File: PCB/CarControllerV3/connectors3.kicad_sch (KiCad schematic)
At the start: 41 parts, among them J5 649012227222, J6 61201621621, K2 RT424005, K5 RT424005

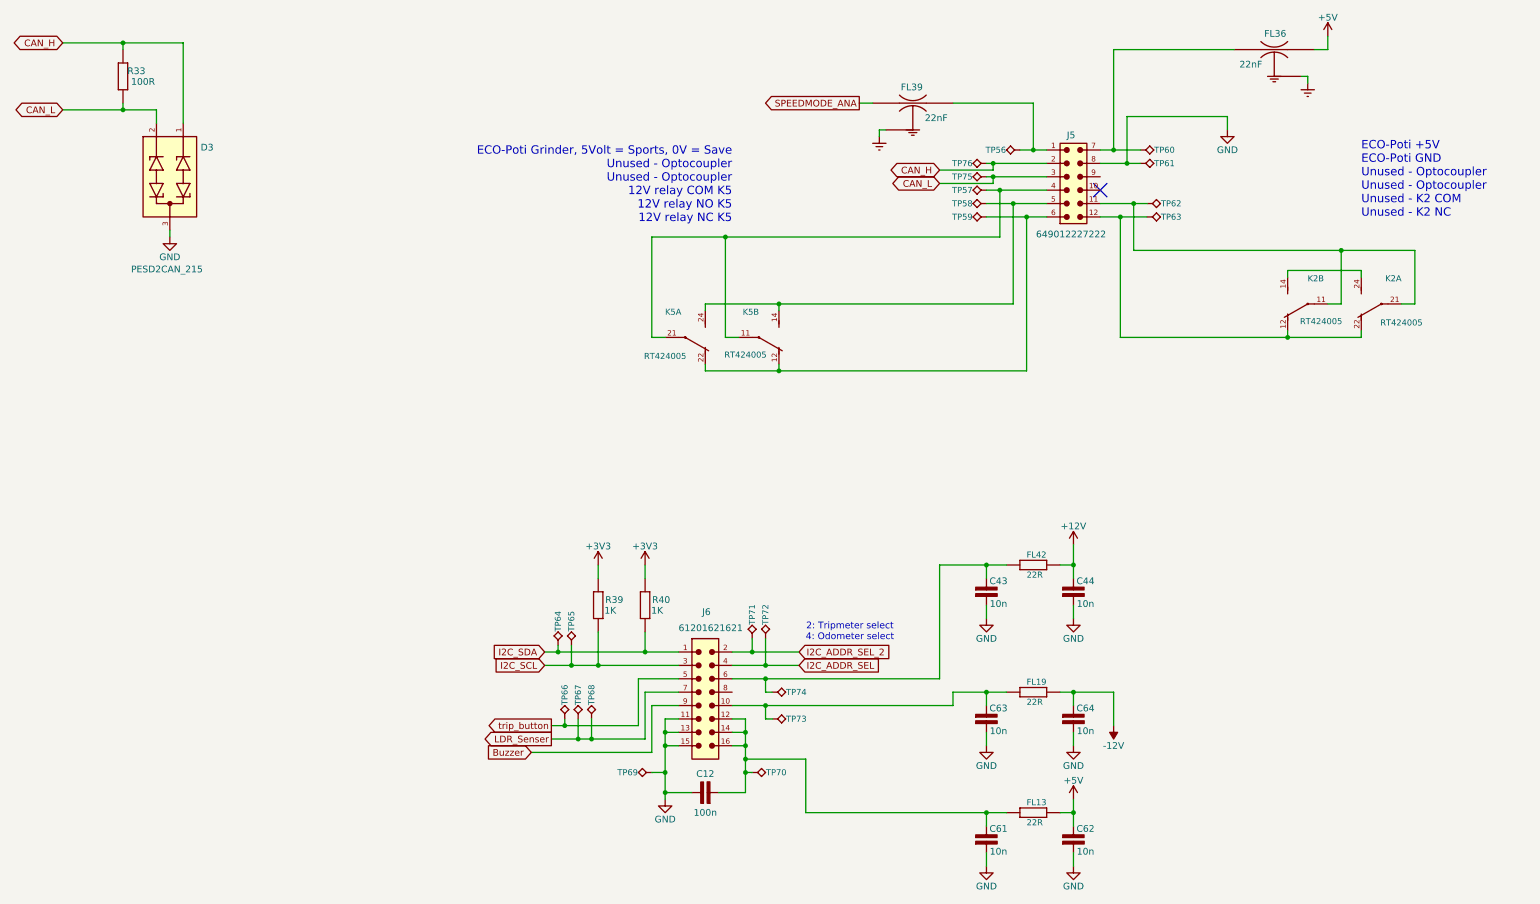
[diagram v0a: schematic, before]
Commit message: More work to PCB
- Rerouted bunch of connections
- Added alternative charge pump circuit
- Bunch of work on analog circuit
- Removed all the capacitor filter on the connectors in favor of filtering when nessesary.
- Placed canbus on JP5.2, JP5.3
- Disconnected various connections that needs to be decided if we should use.
- Added protection to various areas
- Added various todo notes everywhere..
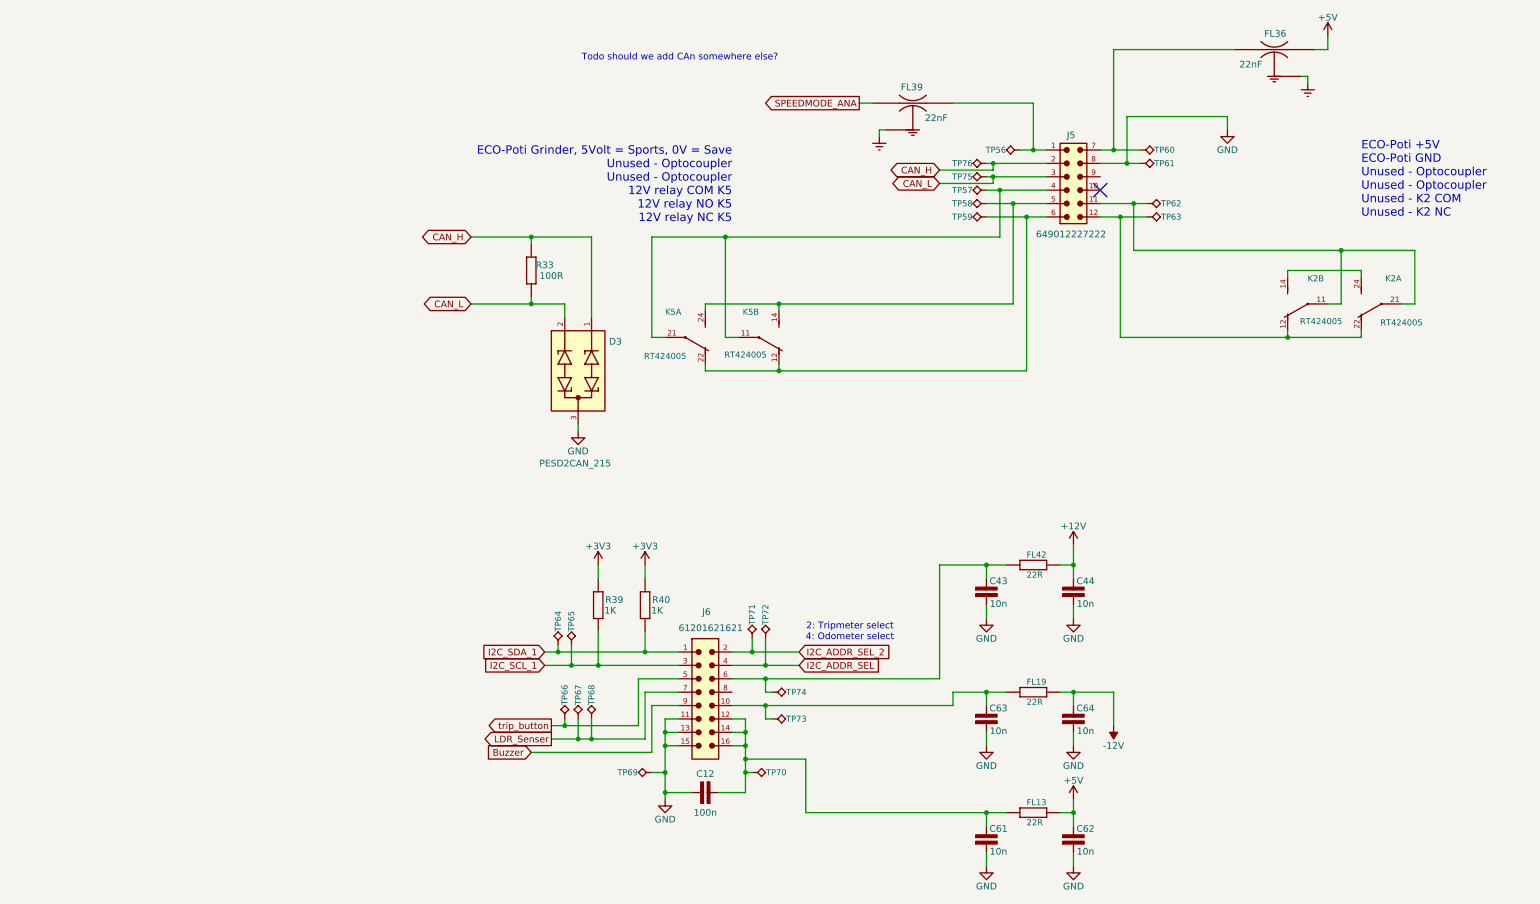
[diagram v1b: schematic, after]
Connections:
- net I2C_SCL renamed I2C_SCL_1
- net I2C_SDA renamed I2C_SDA_1
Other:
- note added: "Todo should we add CAn somewhere else?"
- moved on the sheet: D3, R33
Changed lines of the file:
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@@
 	(generator_version "10.0")
 	(paper "A4")
+	(text "Todo should we add CAn somewhere else?"
+		(exclude_from_sim no)
+		(at 70.104 24.384 0)
+		(effects
+			(font
+				(size 1.27 1.27)
+			)
+		)
+	)
 	(text "ECO-Poti Grinder, 5Volt = Sports, 0V = Save\nUnused - Optocoupler\nUnused - Optocoupler\n12V relay COM K5\n12V relay NO K5\n12V relay NC K5"
 		(exclude_from_sim no)
@@
 	)
 	(junction
-		(at -35.56 21.59)
+		(at 41.91 58.42)
 		(diameter 0)
 		(color 0 0 0 0)
@@
 	)
 	(junction
-		(at -35.56 34.29)
+		(at 41.91 71.12)
 		(diameter 0)
 		(color 0 0 0 0)
@@
 	(wire
 		(pts
-			(xy -29.21 36.83) (xy -29.21 34.29)
+			(xy 48.26 73.66) (xy 48.26 71.12)
 		)
 		(stroke
@@
 	(wire
 		(pts
-			(xy -29.21 34.29) (xy -35.56 34.29)
+			(xy 48.26 71.12) (xy 41.91 71.12)
 		)
 		(stroke
@@
 	(wire
 		(pts
-			(xy -24.13 21.59) (xy -24.13 36.83)
+			(xy 53.34 58.42) (xy 53.34 73.66)
 		)
 		(stroke
@@
 	(wire
 		(pts
-			(xy -35.56 21.59) (xy -24.13 21.59)
+			(xy 41.91 58.42) (xy 53.34 58.42)
 		)
 		(stroke
@@
 	(wire
 		(pts
-			(xy -35.56 34.29) (xy -46.99 34.29)
+			(xy 41.91 71.12) (xy 30.48 71.12)
 		)
 		(stroke
@@
 	(wire
 		(pts
-			(xy -46.99 21.59) (xy -35.56 21.59)
+			(xy 30.48 58.42) (xy 41.91 58.42)
 		)
 		(stroke
@@
 	(wire
 		(pts
-			(xy -35.56 21.59) (xy -35.56 22.86)
+			(xy 41.91 58.42) (xy 41.91 59.69)
 		)
 		(stroke
@@
 	(wire
 		(pts
-			(xy -35.56 33.02) (xy -35.56 34.29)
+			(xy 41.91 69.85) (xy 41.91 71.12)
 		)
 		(stroke
@@
 	(wire
 		(pts
-			(xy -26.67 58.42) (xy -26.67 57.15)
+			(xy 50.8 95.25) (xy 50.8 93.98)
 		)
 		(stroke
@@
 		)
 	)
-	(global_label "I2C_SDA"
+	(global_label "I2C_SDA_1"
 		(shape input)
 		(at 44.45 137.16 180)
@@
 		)
 		(property "Intersheetrefs" "${INTERSHEET_REFS}"
-			(at 33.8448 137.16 0)
+			(at 31.6677 137.16 0)
 			(hide yes)
 			(show_name no)
@@
 	(global_label "CAN_L"
 		(shape bidirectional)
-		(at -46.99 34.29 180)
+		(at 30.48 71.12 180)
 		(fields_autoplaced yes)
 		(effects
@@
 		)
 		(property "Intersheetrefs" "${INTERSHEET_REFS}"
-			(at -56.7713 34.29 0)
+			(at 20.6987 71.12 0)
 			(hide yes)
 			(show_name no)
@@
 		)
 	)
-	(global_label "I2C_SCL"
+	(global_label "I2C_SCL_1"
 		(shape input)
 		(at 44.45 139.7 180)
@@
 		)
 		(property "Intersheetrefs" "${INTERSHEET_REFS}"
-			(at 33.9053 139.7 0)
+			(at 31.7282 139.7 0)
 			(hide yes)
 			(show_name no)
@@
 	(global_label "CAN_H"
 		(shape bidirectional)
-		(at -46.99 21.59 180)
+		(at 30.48 58.42 180)
 		(fields_autoplaced yes)
 		(effects
@@
 		)
 		(property "Intersheetrefs" "${INTERSHEET_REFS}"
-			(at -57.0737 21.59 0)
+			(at 20.3963 58.42 0)
 			(hide yes)
 			(show_name no)
@@
 	(symbol
 		(lib_id "RC0603FR:RC0603FR-07100R")
-		(at -35.56 27.94 90)
+		(at 41.91 64.77 90)
 		(unit 1)
 		(body_style 1)
@@
 		(dnp no)
 		(property "Reference" "R33"
-			(at -33.02 26.924 90)
+			(at 44.45 63.754 90)
 			(show_name no)
 			(do_not_autoplace no)
@@
 		)
 		(property "Value" "100R"
-			(at -31.75 28.956 90)
+			(at 45.72 65.786 90)
 			(show_name no)
 			(do_not_autoplace no)
@@
 		)
 		(property "Footprint" "footprints:RC0603FR-RESC1608X60N"
-			(at -28.575 27.94 0)
+			(at 48.895 64.77 0)
 			(hide yes)
 			(show_name no)
@@
 		)
 		(property "Datasheet" "https://www.farnell.com/datasheets/443971.pdf"
-			(at -26.035 27.94 0)
+			(at 51.435 64.77 0)
 			(hide yes)
 			(show_name no)
@@
 		)
 		(property "Description" "Resistor XXXX 0603 1%"
-			(at -35.56 27.94 0)
+			(at 41.91 64.77 0)
 			(hide yes)
 			(show_name no)
@@
 		)
 		(property "Voltage" "75V"
-			(at -22.225 27.94 0)
+			(at 55.245 64.77 0)
 			(hide yes)
 			(show_name yes)
@@
 		)
 		(property "Tolerance" "1%"
-			(at -20.32 27.94 0)
+			(at 57.15 64.77 0)
 			(hide yes)
 			(show_name yes)
@@
 		)
 		(property "Power" "100mW"
-			(at -18.415 27.94 0)
+			(at 59.055 64.77 0)
 			(hide yes)
 			(show_name yes)
@@
 	(symbol
 		(lib_id "PESD2CAN_215:PESD2CAN_215")
-		(at -26.67 46.99 270)
+		(at 50.8 83.82 270)
 		(unit 1)
 		(body_style 1)
@@
 		(dnp no)
 		(property "Reference" "D3"
-			(at -20.828 42.164 90)
+			(at 56.642 78.994 90)
 			(show_name no)
 			(do_not_autoplace no)
@@
 		)
 		(property "Value" "PESD2CAN_215"
-			(at -34.036 65.278 90)
+			(at 43.434 102.108 90)
 			(show_name no)
 			(do_not_autoplace no)
@@
 		)
 		(property "Footprint" "footprints:IC_PESD2CAN_215"
-			(at -26.67 46.99 0)
+			(at 50.8 83.82 0)
 			(hide yes)
 			(show_name no)
@@
 		)
 		(property "Datasheet" ""
-			(at -26.67 46.99 0)
+			(at 50.8 83.82 0)
 			(hide yes)
 			(show_name no)
@@
 		)
 		(property "Description" ""
-			(at -26.67 46.99 0)
+			(at 50.8 83.82 0)
 			(hide yes)
 			(show_name no)
@@
 		)
 		(property "MF" "Nexperia USA"
-			(at -26.67 46.99 0)
+			(at 50.8 83.82 0)
 			(hide yes)
 			(show_name no)
@@
 		)
 		(property "MAXIMUM_PACKAGE_HEIGHT" "1.1mm"
-			(at -26.67 46.99 0)
+			(at 50.8 83.82 0)
 			(hide yes)
 			(show_name no)
@@
 		)
 		(property "Package" "SOT23-3 Nexperia USA Inc."
-			(at -26.67 46.99 0)
+			(at 50.8 83.82 0)
 			(hide yes)
 			(show_name no)
@@
 		)
 		(property "Price" "None"
-			(at -26.67 46.99 0)
+			(at 50.8 83.82 0)
 			(hide yes)
 			(show_name no)
@@
 		)
 		(property "Check_prices" "https://www.snapeda.com/parts/PESD2CAN,215/Nexperia/view-part/?ref=eda"
-			(at -26.67 46.99 0)
+			(at 50.8 83.82 0)
 			(hide yes)
 			(show_name no)
@@
 		)
 		(property "STANDARD" "Manufacturer Recommendations"
-			(at -26.67 46.99 0)
+			(at 50.8 83.82 0)
 			(hide yes)
 			(show_name no)
@@
 		)
 		(property "PARTREV" "2"
-			(at -26.67 46.99 0)
+			(at 50.8 83.82 0)
 			(hide yes)
 			(show_name no)
@@
 		)
 		(property "SnapEDA_Link" "https://www.snapeda.com/parts/PESD2CAN,215/Nexperia/view-part/?ref=snap"
-			(at -26.67 46.99 0)
+			(at 50.8 83.82 0)
 			(hide yes)
 			(show_name no)
@@
 		)
 		(property "MP" "PESD2CAN,215"
-			(at -26.67 46.99 0)
+			(at 50.8 83.82 0)
 			(hide yes)
 			(show_name no)
@@
 		)
 		(property "Purchase-URL" "https://www.snapeda.com/api/url_track_click_mouser/?unipart_id=422915&manufacturer=Nexperia USA&part_name=PESD2CAN,215&search_term=pesd2can"
-			(at -26.67 46.99 0)
+			(at 50.8 83.82 0)
 			(hide yes)
 			(show_name no)
@@
 		)
 		(property "Description_1" "\n                        \n                            41V Clamp 5A (8/20µs) Ipp Tvs Diode Surface Mount TO-236AB\n                        \n"
-			(at -26.67 46.99 0)
+			(at 50.8 83.82 0)
 			(hide yes)
 			(show_name no)
@@
 		)
 		(property "MANUFACTURER" "Nexperia"
-			(at -26.67 46.99 0)
+			(at 50.8 83.82 0)
 			(hide yes)
 			(show_name no)
@@
 		)
 		(property "Availability" "In Stock"
-			(at -26.67 46.99 0)
+			(at 50.8 83.82 0)
 			(hide yes)
 			(show_name no)
@@
 		)
 		(property "SNAPEDA_PN" "PESD2CAN,215"
-			(at -26.67 46.99 0)
+			(at 50.8 83.82 0)
 			(hide yes)
 			(show_name no)
@@
 	(symbol
 		(lib_id "power:GND")
-		(at -26.67 58.42 0)
+		(at 50.8 95.25 0)
 		(unit 1)
 		(body_style 1)
@@
 		(dnp no)
 		(property "Reference" "#PWR06"
-			(at -26.67 64.77 0)
+			(at 50.8 101.6 0)
 			(hide yes)
 			(show_name no)
@@
 		)
 		(property "Value" "GND"
-			(at -26.67 62.23 0)
+			(at 50.8 99.06 0)
 			(show_name no)
 			(do_not_autoplace no)
@@
 		)
 		(property "Footprint" ""
-			(at -26.67 58.42 0)
+			(at 50.8 95.25 0)
 			(hide yes)
 			(show_name no)
@@
 		)
 		(property "Datasheet" ""
-			(at -26.67 58.42 0)
+			(at 50.8 95.25 0)
 			(hide yes)
 			(show_name no)
@@
 		)
 		(property "Description" "Power symbol creates a global label with name \"GND\" , ground"
-			(at -26.67 58.42 0)
+			(at 50.8 95.25 0)
 			(hide yes)
 			(show_name no)
